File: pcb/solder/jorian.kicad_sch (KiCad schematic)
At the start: 59 parts, among them J1 USB-C Conn, J2 Ex_Bat, Q1 AO3407, SW1 SW_PUSH, SW10 SW_PUSH, SW11 SW_PUSH, SW12 SW_PUSH, SW13 SW_PUSH, SW14 SW_PUSH, SW15 SW_PUSH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

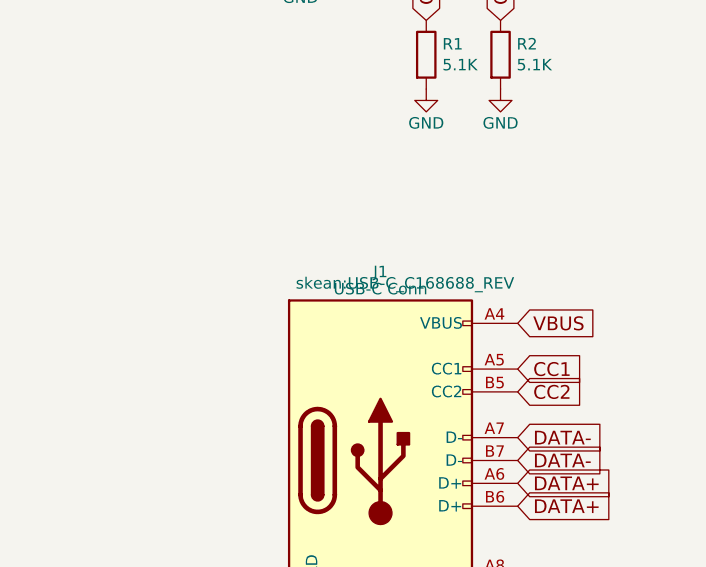
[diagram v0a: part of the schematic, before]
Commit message: Proper library management
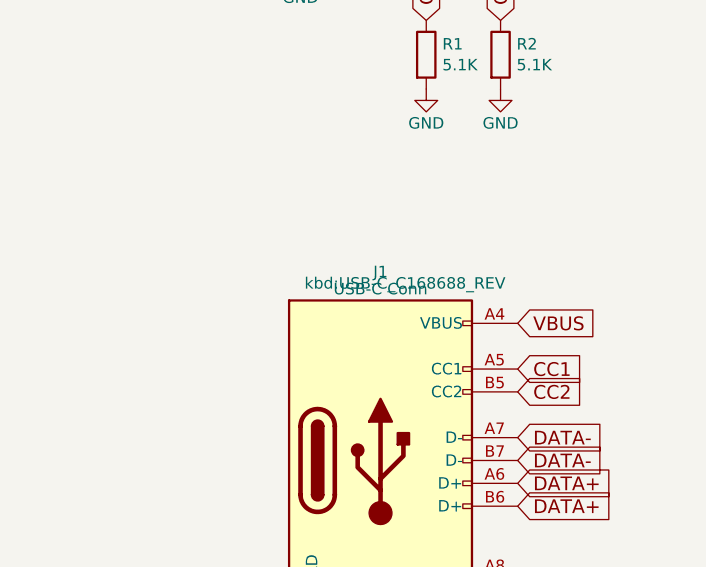
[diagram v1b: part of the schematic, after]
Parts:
- D1, D3: footprint skean:LED_0603_1608Metric_REV -> kbd:LED_0603_1608Metric_REV
- D2: footprint skean:D_SOD-323_HandSoldering_REV -> kbd:D_SOD-323_HandSoldering_REV
- E10, E15, E5: footprint kbd_jorian:edge_conn_ext -> jorian:edge_conn_ext
- E16, E18, E19, E20, E21: footprint kbd:edge_conn -> jorian:edge_conn
- G1, G2: footprint kbd:jorian_logo -> jorian:jorian_logo_840
- J1: footprint skean:USB-C_C168688_REV -> kbd:USB-C_C168688_REV
- J2: footprint skean:Battery_TH -> kbd:Battery_TH
- Q1: footprint skean:SOT-23_Handsoldering_REV -> kbd:SOT-23_Handsoldering_REV
- R1, R2, R3, R4, R5, R6, R7, R8: footprint skean:R_0603_1608Metric_REV -> kbd:R_0603_1608Metric_REV
- RSW1: footprint skean:SW_SPST_EVQP7C_REV -> kbd:SW_SPST_EVQP7C_REV
- SW1, SW10, SW11, SW12, SW13, SW14, SW15, SW16, SW17, SW18, SW19, SW2, SW20, SW21, SW22, SW3, SW4, SW5, SW6, SW7, SW8, SW9: footprint kbd:MX-Alps-1U-REV-TOPOR -> kbd:MX-Alps-Omron-1U-REV
- SW23, SW24: footprint skean:SW_SPDT+H-MSK12C01_hor(7pin_SMD)_REV -> kbd:SW_SPDT+H-MSK12C01_hor(7pin_SMD)_REV
- U2, U3: footprint skean:SOT-23-5_HandSoldering_REV -> kbd:SOT-23-5_HandSoldering_REV

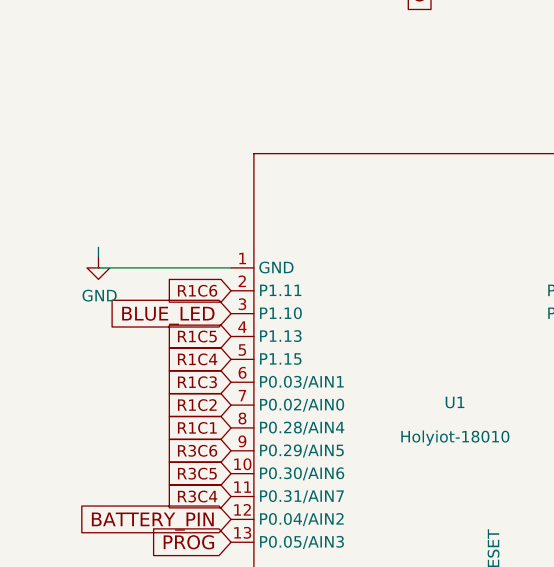
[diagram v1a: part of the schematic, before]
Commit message: Schematic ground fix
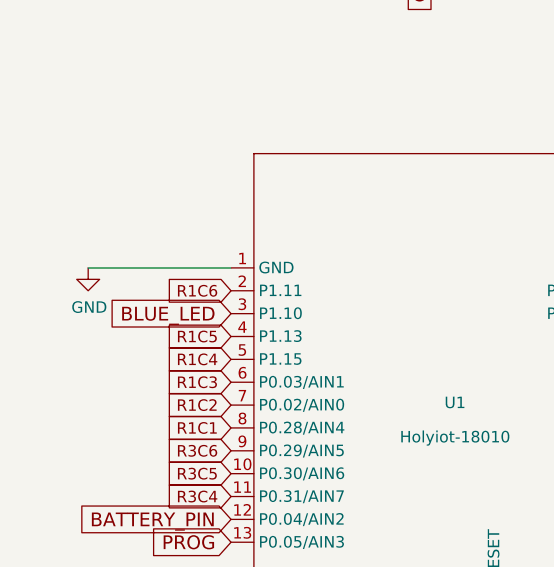
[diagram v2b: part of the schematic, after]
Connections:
- net GND: now also U1.1 (GND)
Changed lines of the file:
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@@
-    (stroke (width 0) (type solid) (color 0 0 0 0))
-  )
-  (wire (pts (xy 18.923 103.124) (xy 18.923 104.14))
     (stroke (width 0) (type solid) (color 0 0 0 0))
   )
@@
     (stroke (width 0) (type solid) (color 0 0 0 0))
   )
-  (wire (pts (xy 33.655 105.41) (xy 18.669 105.41))
-    (stroke (width 0) (type solid) (color 0 0 0 0))
-  )
   (wire (pts (xy 238.76 157.48) (xy 238.76 152.4))
     (stroke (width 0) (type solid) (color 0 0 0 0))
@@
   (wire (pts (xy 139.7 175.895) (xy 139.7 179.705))
     (stroke (width 0) (type solid) (color 0 0 0 0))
+  )
+  (wire (pts (xy 17.78 105.41) (xy 33.655 105.41))
+    (stroke (width 0) (type default) (color 0 0 0 0))
   )
   (wire (pts (xy 96.52 189.865) (xy 99.06 189.865))
@@
     )
   )
-  (symbol (lib_id "power:GND") (at 18.923 104.14 0) (unit 1)
-    (in_bom yes) (on_board yes)
-    (property "Reference" "#PWR021" (id 0) (at 18.923 110.49 0)
-      (effects (font (size 1.27 1.27)) hide)
-    )
-    (property "Value" "GND" (id 1) (at 19.05 108.5342 0))
-    (property "Footprint" "" (id 2) (at 18.923 104.14 0)
-      (effects (font (size 1.27 1.27)) hide)
-    )
-    (property "Datasheet" "" (id 3) (at 18.923 104.14 0)
-      (effects (font (size 1.27 1.27)) hide)
-    )
+  (symbol (lib_id "power:GND") (at 17.78 105.41 0) (unit 1)
+    (in_bom yes) (on_board yes)
+    (property "Reference" "#PWR021" (id 0) (at 17.78 111.76 0)
+      (effects (font (size 1.27 1.27)) hide)
+    )
+    (property "Value" "GND" (id 1) (at 17.907 109.8042 0))
+    (property "Footprint" "" (id 2) (at 17.78 105.41 0)
+      (effects (font (size 1.27 1.27)) hide)
+    )
+    (property "Datasheet" "" (id 3) (at 17.78 105.41 0)
+      (effects (font (size 1.27 1.27)) hide)
+    )
